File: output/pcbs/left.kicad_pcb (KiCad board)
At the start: 2 copper layers, 132 x 103 mm, 45 parts

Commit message: can't believe that worked
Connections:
- D1 pad 1: (no net) -> P6
- D10 pad 1: (no net) -> P6
- D11 pad 1: (no net) -> P7
- D12 pad 1: (no net) -> P8
- D13 pad 1: (no net) -> P6
- D14 pad 1: (no net) -> P7
- D15 pad 1: (no net) -> P8
- D16 pad 1: (no net) -> P6
- D17 pad 1: (no net) -> P7
- D18 pad 1: (no net) -> P8
- D19 pad 1: (no net) -> P6
- D2 pad 1: (no net) -> P7
- D20 pad 1: (no net) -> P7
- D21 pad 1: (no net) -> P6
- D22 pad 1: (no net) -> P7
- D3 pad 1: (no net) -> P8
- D4 pad 1: (no net) -> P6
- D5 pad 1: (no net) -> P7
- D6 pad 1: (no net) -> P8
- D7 pad 1: (no net) -> P6
- D8 pad 1: (no net) -> P7
- D9 pad 1: (no net) -> P8

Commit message: reroute and do some other stuff I honestly forgot
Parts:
- moved S22 8.84 mm to (108.1, 17.2), turned to -20 degrees
- moved D22 7.71 mm to (106.4, 21.9), turned to -20 degrees
- moved D21 6.49 mm to (100.2, 38.9), turned to -20 degrees
- moved S21 6.25 mm to (101.9, 34.2), turned to -20 degrees
- moved S20 6.25 mm to (91.2, 11.1), turned to -20 degrees
- moved D20 4.51 mm to (89.4, 15.8), turned to -20 degrees
- moved D19 1.74 mm to (83.3, 32.7), turned to -20 degrees
- turned S19 to -20 degrees
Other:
- board size 132 x 103 mm -> 133.2 x 112.3 mm

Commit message: im tired of giving things names
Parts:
- moved D12 2.00 mm to (54.0, -46.0)
- moved D15 2.00 mm to (72.0, -40.0)
- moved D18 2.00 mm to (90.0, -40.0)
- moved D3 2.00 mm to (0.00, -29.0)
- moved D6 2.00 mm to (18.0, -29.0)
- moved D9 2.00 mm to (36.0, -41.0)
- moved MCU1 2.00 mm to (110.0, -51.0)
- moved S12 2.00 mm to (54.0, -51.0)
- moved S15 2.00 mm to (72.0, -45.0)
- moved S18 2.00 mm to (90.0, -45.0)
- moved S3 2.00 mm to (0.00, -34.0)
- moved S6 2.00 mm to (18.0, -34.0)
- moved S9 2.00 mm to (36.0, -46.0)
- moved D11 1.00 mm to (54.0, -29.0)
- moved D14 1.00 mm to (72.0, -23.0)
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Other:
- board size 133.2 x 112.3 mm -> 132.7 x 109.8 mm

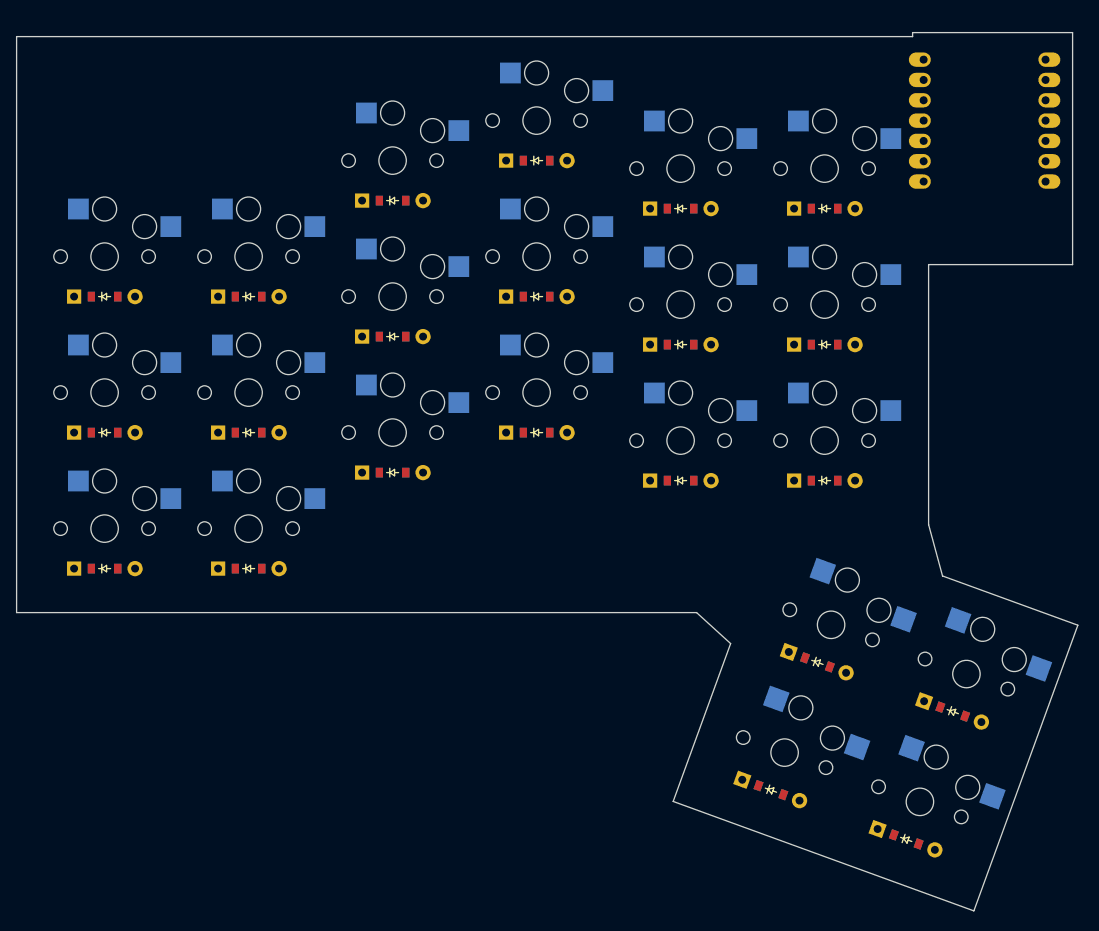
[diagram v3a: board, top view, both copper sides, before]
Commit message: use cleoloide footprints
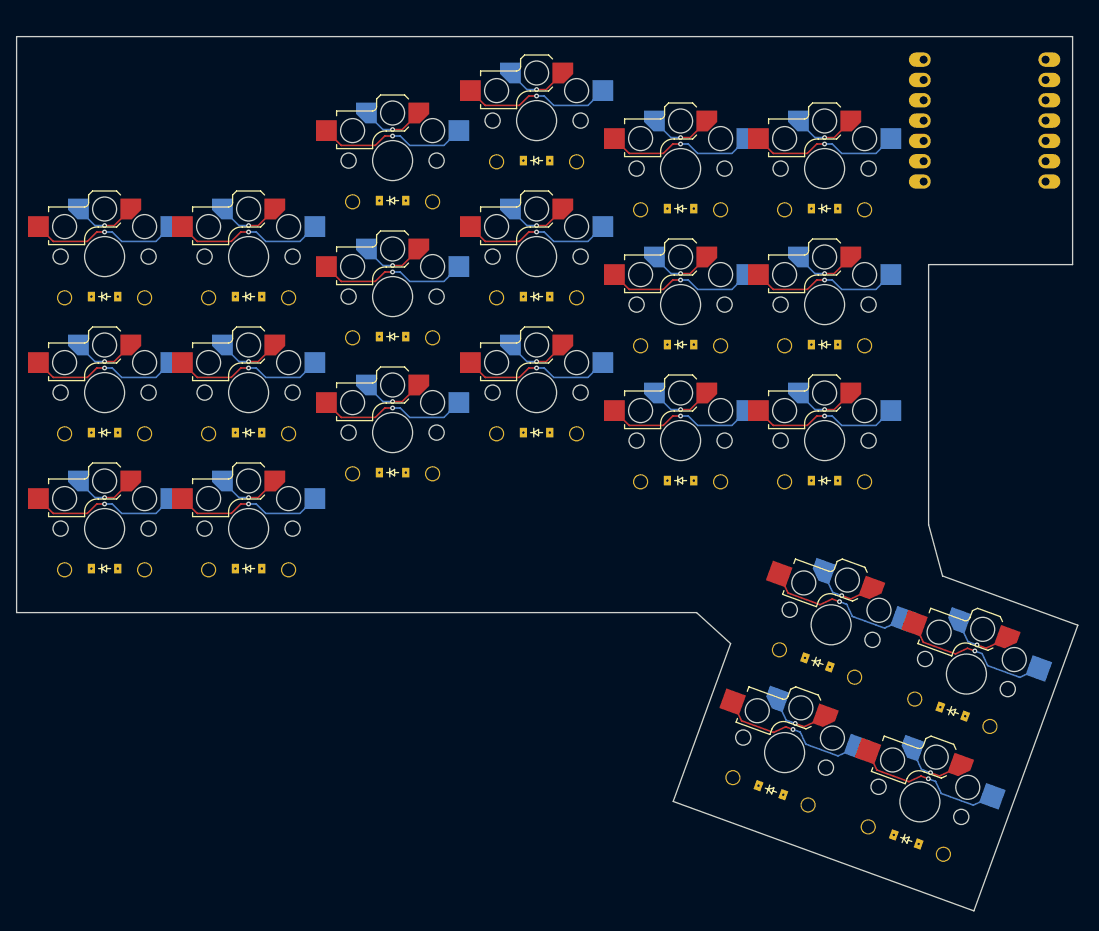
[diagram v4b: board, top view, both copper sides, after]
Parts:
- D1, D10, D11, D12, D13, D14, D15, D16, D17, D18, D19, D2, D20, D21, D22, D3, D4, D5, D6, D7, D8, D9: footprint ComboDiode -> ceoloide:diode_tht_sod123
- S1, S10, S11, S12, S13, S14, S15, S16, S17, S18, S19, S2, S20, S21, S22, S3, S4, S5, S6, S7, S8, S9: footprint PG1350 -> ceoloide:switch_choc_v1_v2; moved to B.Cu
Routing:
- net P5: track 0.00 -> 24.8 mm, vias 0 -> 3
- net P4: track 0.00 -> 24.8 mm, vias 0 -> 3
- net P3: track 0.00 -> 24.8 mm, vias 0 -> 3
- net P2: track 0.00 -> 24.8 mm, vias 0 -> 3
- net P1: track 0.00 -> 24.8 mm, vias 0 -> 3
- net P0: track 0.00 -> 24.8 mm, vias 0 -> 3
- net inner_top: track 0.00 -> 19.1 mm, vias 0 -> 1
- net inner_home: track 0.00 -> 19.1 mm, vias 0 -> 1
- net inner_bottom: track 0.00 -> 19.1 mm, vias 0 -> 1
- net index_top: track 0.00 -> 19.1 mm, vias 0 -> 1
- net index_home: track 0.00 -> 19.1 mm, vias 0 -> 1
- net index_bottom: track 0.00 -> 19.1 mm, vias 0 -> 1
- net ring_top: track 0.00 -> 19.1 mm, vias 0 -> 1
- net ring_home: track 0.00 -> 19.1 mm, vias 0 -> 1
- net pinky_top: track 0.00 -> 19.1 mm, vias 0 -> 1
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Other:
- board size 132.7 x 109.8 mm -> 132.7 x 109.3 mm
- net class Default removed

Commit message: ya
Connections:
- D1 pad 1: P6 -> P8
- D10 pad 1: P6 -> P8
- D12 pad 1: P8 -> P6
- D13 pad 1: P6 -> P8
- D15 pad 1: P8 -> P6
- D16 pad 1: P6 -> P8
- D18 pad 1: P8 -> P6
- D19 pad 1: P6 -> P8
- D21 pad 1: P6 -> P8
- D3 pad 1: P8 -> P6
- D4 pad 1: P6 -> P8
- D6 pad 1: P8 -> P6
- D7 pad 1: P6 -> P8
- D9 pad 1: P8 -> P6
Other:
- outline, holes or cut-outs redrawn
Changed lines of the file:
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@@
 (net 32 "right_bottom")
 (net 33 "right_top")
-(net 34 "P6")
+(net 34 "P8")
 (net 35 "P7")
-(net 36 "P8")
+(net 36 "P6")
 (net 37 "RAW5V")
 (net 38 "RAW3V3")
@@
         )
       )
-      (pad "1" thru_hole rect (at -1.65 0 0) (size 0.9 1.2) (drill 0.3) (layers "*.Cu" "*.Paste" "*.Mask") (net 34 "P6"))
+      (pad "1" thru_hole rect (at -1.65 0 0) (size 0.9 1.2) (drill 0.3) (layers "*.Cu" "*.Paste" "*.Mask") (net 34 "P8"))
       (pad "2" thru_hole rect (at 1.65 0 0) (size 0.9 1.2) (drill 0.3) (layers "*.Cu" "*.Paste" "*.Mask") (net 2 "outer_bottom"))
     )
@@
         )
       )
-      (pad "1" thru_hole rect (at -1.65 0 0) (size 0.9 1.2) (drill 0.3) (layers "*.Cu" "*.Paste" "*.Mask") (net 36 "P8"))
+      (pad "1" thru_hole rect (at -1.65 0 0) (size 0.9 1.2) (drill 0.3) (layers "*.Cu" "*.Paste" "*.Mask") (net 36 "P6"))
       (pad "2" thru_hole rect (at 1.65 0 0) (size 0.9 1.2) (drill 0.3) (layers "*.Cu" "*.Paste" "*.Mask") (net 7 "outer_top"))
     )
@@
         )
       )
-      (pad "1" thru_hole rect (at -1.65 0 0) (size 0.9 1.2) (drill 0.3) (layers "*.Cu" "*.Paste" "*.Mask") (net 34 "P6"))
+      (pad "1" thru_hole rect (at -1.65 0 0) (size 0.9 1.2) (drill 0.3) (layers "*.Cu" "*.Paste" "*.Mask") (net 34 "P8"))
       (pad "2" thru_hole rect (at 1.65 0 0) (size 0.9 1.2) (drill 0.3) (layers "*.Cu" "*.Paste" "*.Mask") (net 9 "pinky_bottom"))
     )
@@
         )
       )
-      (pad "1" thru_hole rect (at -1.65 0 0) (size 0.9 1.2) (drill 0.3) (layers "*.Cu" "*.Paste" "*.Mask") (net 36 "P8"))
+      (pad "1" thru_hole rect (at -1.65 0 0) (size 0.9 1.2) (drill 0.3) (layers "*.Cu" "*.Paste" "*.Mask") (net 36 "P6"))
       (pad "2" thru_hole rect (at 1.65 0 0) (size 0.9 1.2) (drill 0.3) (layers "*.Cu" "*.Paste" "*.Mask") (net 11 "pinky_top"))
     )
@@
         )
       )
-      (pad "1" thru_hole rect (at -1.65 0 0) (size 0.9 1.2) (drill 0.3) (layers "*.Cu" "*.Paste" "*.Mask") (net 34 "P6"))
+      (pad "1" thru_hole rect (at -1.65 0 0) (size 0.9 1.2) (drill 0.3) (layers "*.Cu" "*.Paste" "*.Mask") (net 34 "P8"))
       (pad "2" thru_hole rect (at 1.65 0 0) (size 0.9 1.2) (drill 0.3) (layers "*.Cu" "*.Paste" "*.Mask") (net 13 "ring_bottom"))
     )
@@
         )
       )
-      (pad "1" thru_hole rect (at -1.65 0 0) (size 0.9 1.2) (drill 0.3) (layers "*.Cu" "*.Paste" "*.Mask") (net 36 "P8"))
+      (pad "1" thru_hole rect (at -1.65 0 0) (size 0.9 1.2) (drill 0.3) (layers "*.Cu" "*.Paste" "*.Mask") (net 36 "P6"))
       (pad "2" thru_hole rect (at 1.65 0 0) (size 0.9 1.2) (drill 0.3) (layers "*.Cu" "*.Paste" "*.Mask") (net 15 "ring_top"))
     )
@@
         )
       )
-      (pad "1" thru_hole rect (at -1.65 0 0) (size 0.9 1.2) (drill 0.3) (layers "*.Cu" "*.Paste" "*.Mask") (net 34 "P6"))
+      (pad "1" thru_hole rect (at -1.65 0 0) (size 0.9 1.2) (drill 0.3) (layers "*.Cu" "*.Paste" "*.Mask") (net 34 "P8"))
       (pad "2" thru_hole rect (at 1.65 0 0) (size 0.9 1.2) (drill 0.3) (layers "*.Cu" "*.Paste" "*.Mask") (net 17 "middle_bottom"))
     )
@@
         )
       )
-      (pad "1" thru_hole rect (at -1.65 0 0) (size 0.9 1.2) (drill 0.3) (layers "*.Cu" "*.Paste" "*.Mask") (net 36 "P8"))
+      (pad "1" thru_hole rect (at -1.65 0 0) (size 0.9 1.2) (drill 0.3) (layers "*.Cu" "*.Paste" "*.Mask") (net 36 "P6"))
       (pad "2" thru_hole rect (at 1.65 0 0) (size 0.9 1.2) (drill 0.3) (layers "*.Cu" "*.Paste" "*.Mask") (net 19 "middle_top"))
     )
@@
         )
       )
-      (pad "1" thru_hole rect (at -1.65 0 0) (size 0.9 1.2) (drill 0.3) (layers "*.Cu" "*.Paste" "*.Mask") (net 34 "P6"))
+      (pad "1" thru_hole rect (at -1.65 0 0) (size 0.9 1.2) (drill 0.3) (layers "*.Cu" "*.Paste" "*.Mask") (net 34 "P8"))
       (pad "2" thru_hole rect (at 1.65 0 0) (size 0.9 1.2) (drill 0.3) (layers "*.Cu" "*.Paste" "*.Mask") (net 21 "index_bottom"))
     )
@@
         )
       )
-      (pad "1" thru_hole rect (at -1.65 0 0) (size 0.9 1.2) (drill 0.3) (layers "*.Cu" "*.Paste" "*.Mask") (net 36 "P8"))
+      (pad "1" thru_hole rect (at -1.65 0 0) (size 0.9 1.2) (drill 0.3) (layers "*.Cu" "*.Paste" "*.Mask") (net 36 "P6"))
       (pad "2" thru_hole rect (at 1.65 0 0) (size 0.9 1.2) (drill 0.3) (layers "*.Cu" "*.Paste" "*.Mask") (net 23 "index_top"))
     )
@@
         )
       )
-      (pad "1" thru_hole rect (at -1.65 0 0) (size 0.9 1.2) (drill 0.3) (layers "*.Cu" "*.Paste" "*.Mask") (net 34 "P6"))
+      (pad "1" thru_hole rect (at -1.65 0 0) (size 0.9 1.2) (drill 0.3) (layers "*.Cu" "*.Paste" "*.Mask") (net 34 "P8"))
       (pad "2" thru_hole rect (at 1.65 0 0) (size 0.9 1.2) (drill 0.3) (layers "*.Cu" "*.Paste" "*.Mask") (net 25 "inner_bottom"))
     )
@@
         )
       )
-      (pad "1" thru_hole rect (at -1.65 0 0) (size 0.9 1.2) (drill 0.3) (layers "*.Cu" "*.Paste" "*.Mask") (net 36 "P8"))
+      (pad "1" thru_hole rect (at -1.65 0 0) (size 0.9 1.2) (drill 0.3) (layers "*.Cu" "*.Paste" "*.Mask") (net 36 "P6"))
       (pad "2" thru_hole rect (at 1.65 0 0) (size 0.9 1.2) (drill 0.3) (layers "*.Cu" "*.Paste" "*.Mask") (net 27 "inner_top"))
     )
@@
         )
       )
-      (pad "1" thru_hole rect (at -1.65 0 -20) (size 0.9 1.2) (drill 0.3) (layers "*.Cu" "*.Paste" "*.Mask") (net 34 "P6"))
+      (pad "1" thru_hole rect (at -1.65 0 -20) (size 0.9 1.2) (drill 0.3) (layers "*.Cu" "*.Paste" "*.Mask") (net 34 "P8"))
       (pad "2" thru_hole rect (at 1.65 0 -20) (size 0.9 1.2) (drill 0.3) (layers "*.Cu" "*.Paste" "*.Mask") (net 29 "left_bottom"))
     )
@@
         )
       )
-      (pad "1" thru_hole rect (at -1.65 0 -20) (size 0.9 1.2) (drill 0.3) (layers "*.Cu" "*.Paste" "*.Mask") (net 34 "P6"))
+      (pad "1" thru_hole rect (at -1.65 0 -20) (size 0.9 1.2) (drill 0.3) (layers "*.Cu" "*.Paste" "*.Mask") (net 34 "P8"))
       (pad "2" thru_hole rect (at 1.65 0 -20) (size 0.9 1.2) (drill 0.3) (layers "*.Cu" "*.Paste" "*.Mask") (net 32 "right_bottom"))
     )
@@
       (fp_rect (start -5.285811 -6.785813) (end -3.507811 -4.118813) (layer Dwgs.User) (width 0.12) (fill none))
       (fp_rect (start 3.350197 -10.849813) (end 5.128197 -8.182813) (layer Dwgs.User) (width 0.12) (fill none))
+      (fp_rect
+        (start -6 -3)
+        (end 0 3)
+        (stroke (width 0.12) (type default))
+        (fill none)
+        (layer Edge.Cuts)
+      )
       (pad "1" thru_hole oval (at -7.62 -7.62 0) (size 2.75 1.8) (drill 1 (offset -0.475 0)) (layers *.Cu *.Mask) (net 1 "P0"))
       (pad "2" thru_hole oval (at -7.62 -5.08 0) (size 2.75 1.8) (drill 1 (offset -0.475 0)) (layers *.Cu *.Mask) (net 8 "P1"))
@@
       (pad "5" thru_hole oval (at -7.62 2.54 0) (size 2.75 1.8) (drill 1 (offset -0.475 0)) (layers *.Cu *.Mask) (net 20 "P4"))
       (pad "6" thru_hole oval (at -7.62 5.08 0) (size 2.75 1.8) (drill 1 (offset -0.475 0)) (layers *.Cu *.Mask) (net 24 "P5"))
-      (pad "7" thru_hole oval (at -7.62 7.62 0) (size 2.75 1.8) (drill 1 (offset -0.475 0)) (layers *.Cu *.Mask) (net 34 "P6"))
+      (pad "7" thru_hole oval (at -7.62 7.62 0) (size 2.75 1.8) (drill 1 (offset -0.475 0)) (layers *.Cu *.Mask) (net 36 "P6"))
       (pad "8" thru_hole oval (at 7.62 7.62 180) (size 2.75 1.8) (drill 1 (offset -0.475 0)) (layers *.Cu *.Mask) (net 35 "P7"))
-      (pad "9" thru_hole oval (at 7.62 5.08 180) (size 2.75 1.8) (drill 1 (offset -0.475 0)) (layers *.Cu *.Mask) (net 36 "P8"))
+      (pad "9" thru_hole oval (at 7.62 5.08 180) (size 2.75 1.8) (drill 1 (offset -0.475 0)) (layers *.Cu *.Mask) (net 34 "P8"))
       (pad "10" thru_hole oval (at 7.62 2.54 180) (size 2.75 1.8) (drill 1 (offset -0.475 0)) (layers *.Cu *.Mask) (net 28 "P9"))
       (pad "11" thru_hole oval (at 7.62 0 180) (size 2.75 1.8) (drill 1 (offset -0.475 0)) (layers *.Cu *.Mask) (net 31 "P10"))
@@
       (pad "14" thru_hole oval (at 7.62 -7.62 180) (size 2.75 1.8) (drill 1 (offset -0.475 0)) (layers *.Cu *.Mask) (net 37 "RAW5V"))
     )
-  (gr_line (start 103 -0.5) (end 103 -33) (layer Edge.Cuts) (stroke (width 0.15) (type default)))
+  (gr_line (start 101 -0.5) (end 101 -38) (layer Edge.Cuts) (stroke (width 0.15) (type default)))
 (gr_line (start -11 -61.5) (end 121 -61.5) (layer Edge.Cuts) (stroke (width 0.15) (type default)))
 (gr_line (start -11 -61.5) (end -11 10.5) (layer Edge.Cuts) (stroke (width 0.15) (type default)))
@@
 (gr_line (start 108.6598745 47.7853567) (end 121.6566399 12.077037100000002) (layer Edge.Cuts) (stroke (width 0.15) (type default)))
 (gr_line (start 121.6566399 12.077037100000002) (end 104.7421727 5.9206745000000005) (layer Edge.Cuts) (stroke (width 0.15) (type default)))
-(gr_line (start 104.7421727 5.9206745000000005) (end 103 -0.5) (layer Edge.Cuts) (stroke (width 0.15) (type default)))
-(gr_line (start 103 -33) (end 121 -33) (layer Edge.Cuts) (stroke (width 0.15) (type default)))
-(gr_line (start 121 -33) (end 121 -61.5) (layer Edge.Cuts) (stroke (width 0.15) (type default)))
+(gr_line (start 104.7421727 5.9206745000000005) (end 101 -0.5) (layer Edge.Cuts) (stroke (width 0.15) (type default)))
+(gr_line (start 101 -38) (end 121 -38) (layer Edge.Cuts) (stroke (width 0.15) (type default)))
+(gr_line (start 121 -38) (end 121 -61.5) (layer Edge.Cuts) (stroke (width 0.15) (type default)))
 )
